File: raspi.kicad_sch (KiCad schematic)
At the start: 0 parts

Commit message: Updated schematics
Added the input current sense, expansion header and various test points.
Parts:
- added J8: Conn_01x03, symbol Connector_Generic:Conn_01x03
- added R24, R25, R26, R27: 0, symbol Device:R_Small_US
- added U6: RP2350B-QFN80, symbol rp2350b-qfn80:RP2350B-QFN80
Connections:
- new net Debug_RX: J8.1 (Pin_1), R24.2
- new net Debug_TX: J8.2 (Pin_2), R25.1
- new net Expansion_RX: R26.1
- new net Expansion_TX: R27.2
- new net GND: J8.3 (Pin_3)
- new net Raspi_RX: R24.1, R27.1
- new net Raspi_TX: R25.2, R26.2

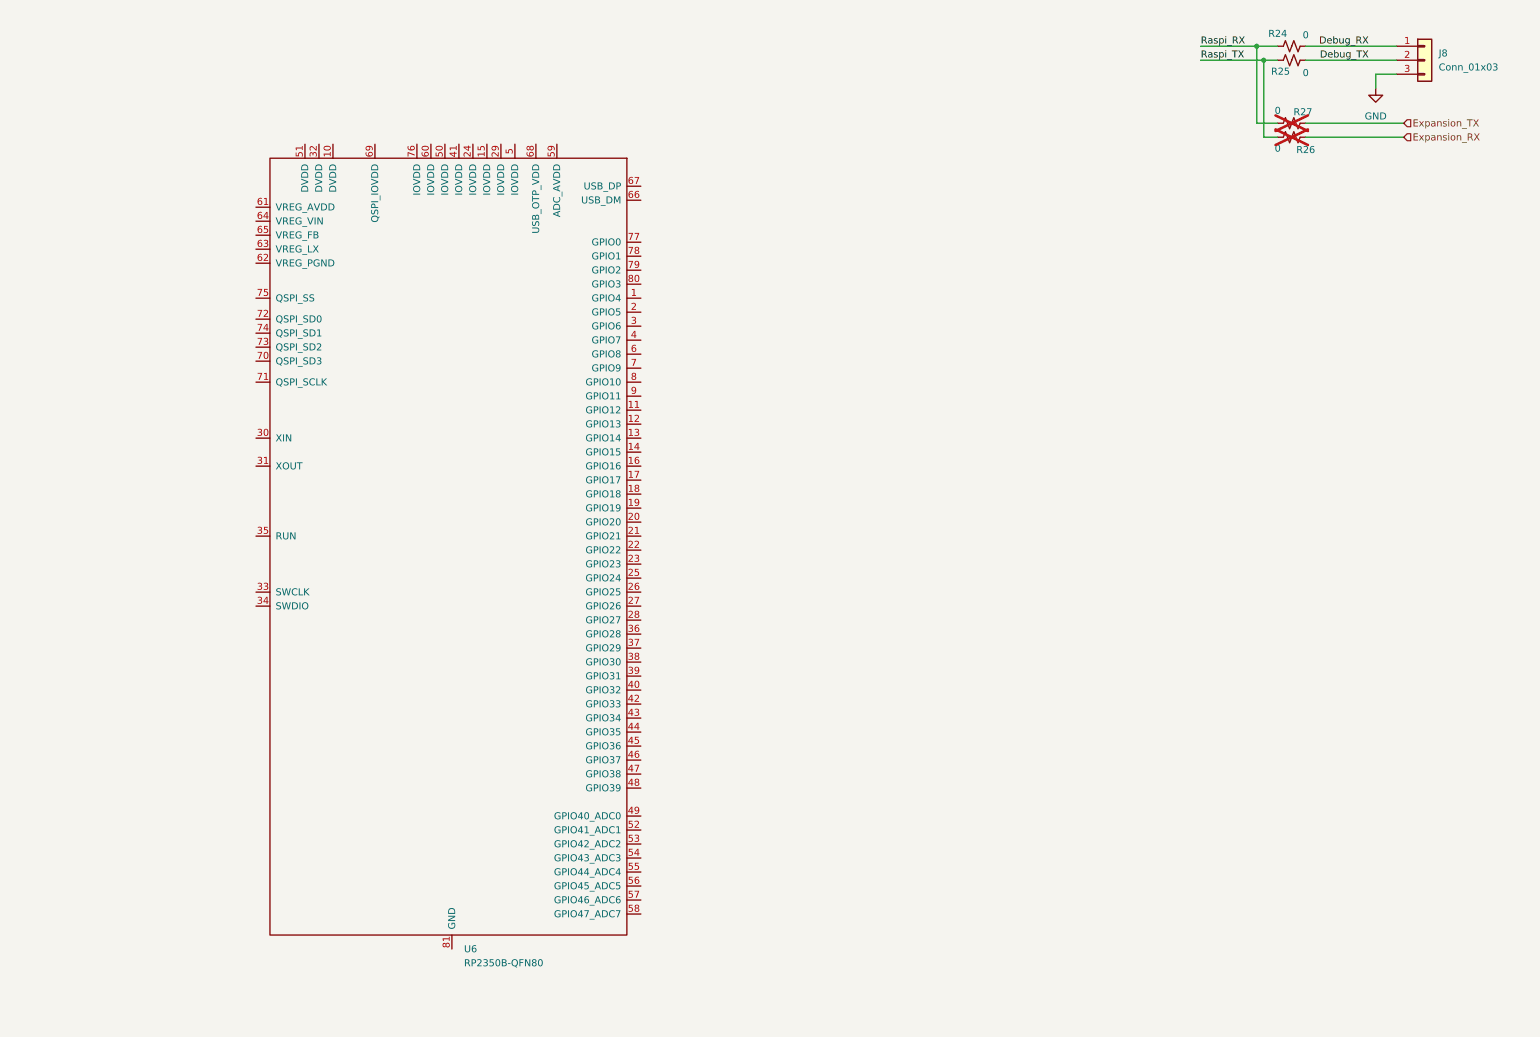
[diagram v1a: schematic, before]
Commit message: Added RPI stuff
Added power passives and usb passives
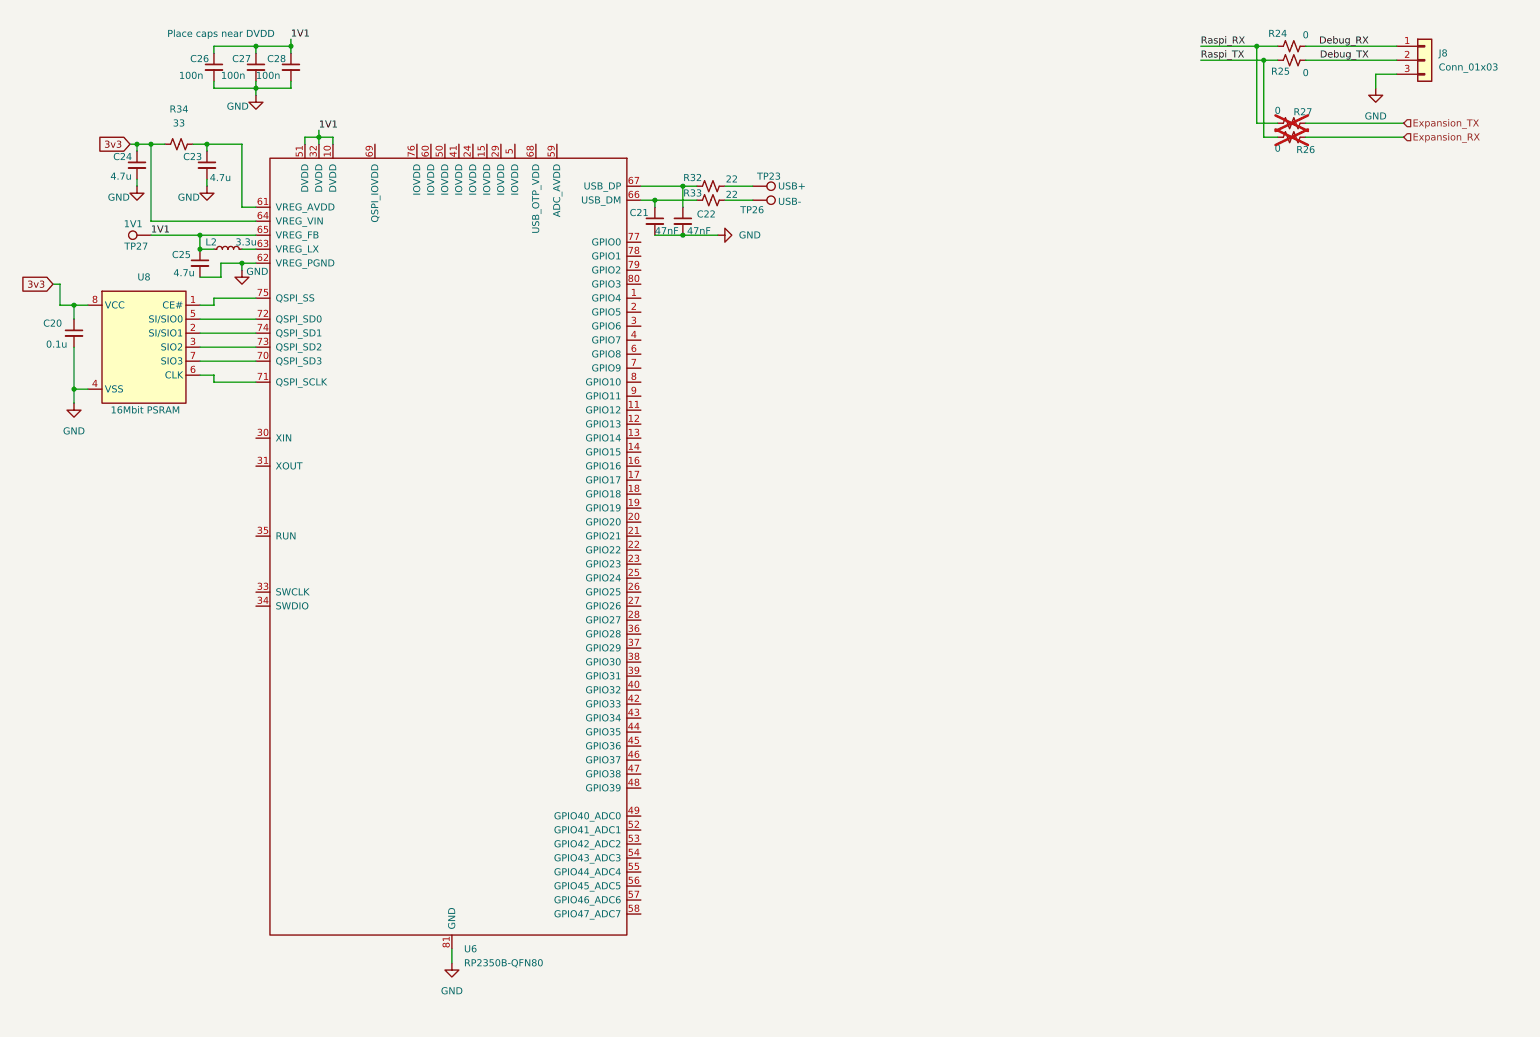
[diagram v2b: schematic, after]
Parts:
- added C20: 0.1u, symbol Device:C_Small
- added C21, C22: 47nF, symbol Device:C_Small
- added C23, C24, C25: 4.7u, symbol Device:C_Small
- added C26, C27, C28: 100n, symbol Device:C_Small
- added L2: 3.3u, symbol Device:L_Small
- added R32, R33: 22, symbol Device:R_Small_US
- added R34: 33, symbol Device:R_Small_US
- added TP23: USB+, symbol Connector:TestPoint
- added TP26: USB-, symbol Connector:TestPoint
- added TP27: 1V1, symbol Connector:TestPoint
- added U8: 16Mbit PSRAM, symbol IS6xWVS2M8xLL:IS6xWVS2M8xLL
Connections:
- net GND: now also U6.62 (VREG_PGND), U6.81 (GND), C20.2, C21.2, C22.2, C23.2, C24.2, C25.2, C26.2, C27.2, C28.2, U8.4 (VSS)
- net 1V1: now reaches U6.10 (DVDD)
- net 1V1: now also U6.32 (DVDD), U6.51 (DVDD), U6.65 (VREG_FB), C25.1, C26.1, C27.1, C28.1, L2.1, TP27.1
- net at U6.61 (VREG_AVDD): now also C23.1, R34.2
- net at U6.63 (VREG_LX): now also L2.2
- net 3v3: now reaches U6.64 (VREG_VIN)
- net 3v3: now also C20.1, C24.1, R34.1, U8.8 (VCC)
- net at U6.66 (USB_DM): now also C21.1, R33.1
- net at U6.67 (USB_DP): now also C22.1, R32.1
- net at U6.70 (QSPI_SD3): now also U8.7 (SIO3)
- net at U6.71 (QSPI_SCLK): now also U8.6 (CLK)
- net at U6.72 (QSPI_SD0): now also U8.5 (SI/SIO0)
- net at U6.73 (QSPI_SD2): now also U8.3 (SIO2)
- net at U6.74 (QSPI_SD1): now also U8.2 (SI/SIO1)
- net at U6.75 (QSPI_SS): now also U8.1 (CE#)
- new net: R32.2, TP23.1
- new net: R33.2, TP26.1
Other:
- note added: "Place caps near DVDD"

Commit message: Setup top sheet
Added TVS diodes, updated top sheet, misc label fixes
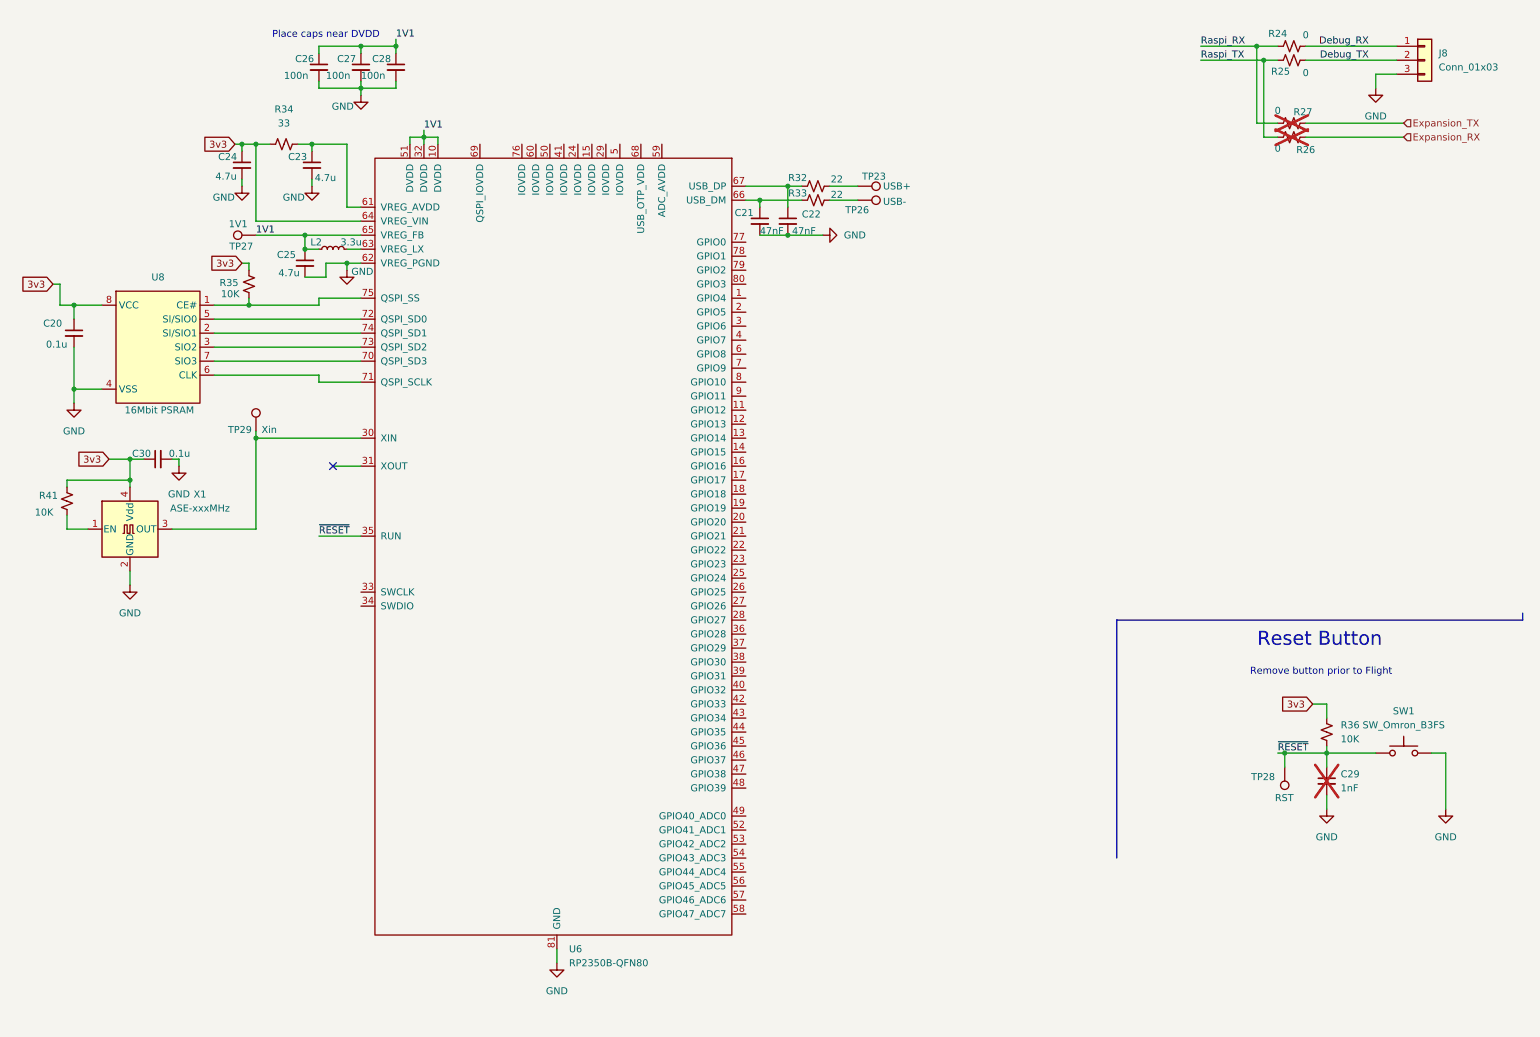
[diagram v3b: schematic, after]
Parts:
- added C29: 1nF, symbol Device:C_Small
- added C30: 0.1u, symbol Device:C_Small
- added R35, R36, R41: 10K, symbol Device:R_Small_US
- added SW1: SW_Omron_B3FS, symbol Switch:SW_Omron_B3FS
- added TP28: RST, symbol Connector:TestPoint
- added TP29: Xin, symbol Connector:TestPoint
- added X1: ASE-xxxMHz, Oscillator:Oscillator_SMD_Abracon_ASE-4Pin_3.2x2.5mm, symbol Oscillator:ASE-xxxMHz
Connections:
- net 3v3: now also C30.1, R35.1, R36.1, R41.1, X1.4 (Vdd)
- net GND: now also C29.2, C30.2, SW1.2, X1.2 (GND)
- net at U6.30 (XIN): now also TP29.1, X1.3 (OUT)
- net ~{RESET}: now reaches U6.35 (RUN)
- net ~{RESET}: now also C29.1, R36.2, SW1.1, TP28.1
- net at U6.75 (QSPI_SS), U8.1 (CE#): now also R35.2
- new net: R41.2, X1.1 (EN)
- no-connect marks 0 -> 1
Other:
- note added: "Remove button prior to Flight"
- note added: "Reset Button"
- moved on the sheet: C21, C22, C23, C24, C25, C26, C27, C28, L2, R32, R33, R34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

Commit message: Updated Raspi Sheet
Added hierarchical labels and misc additions.
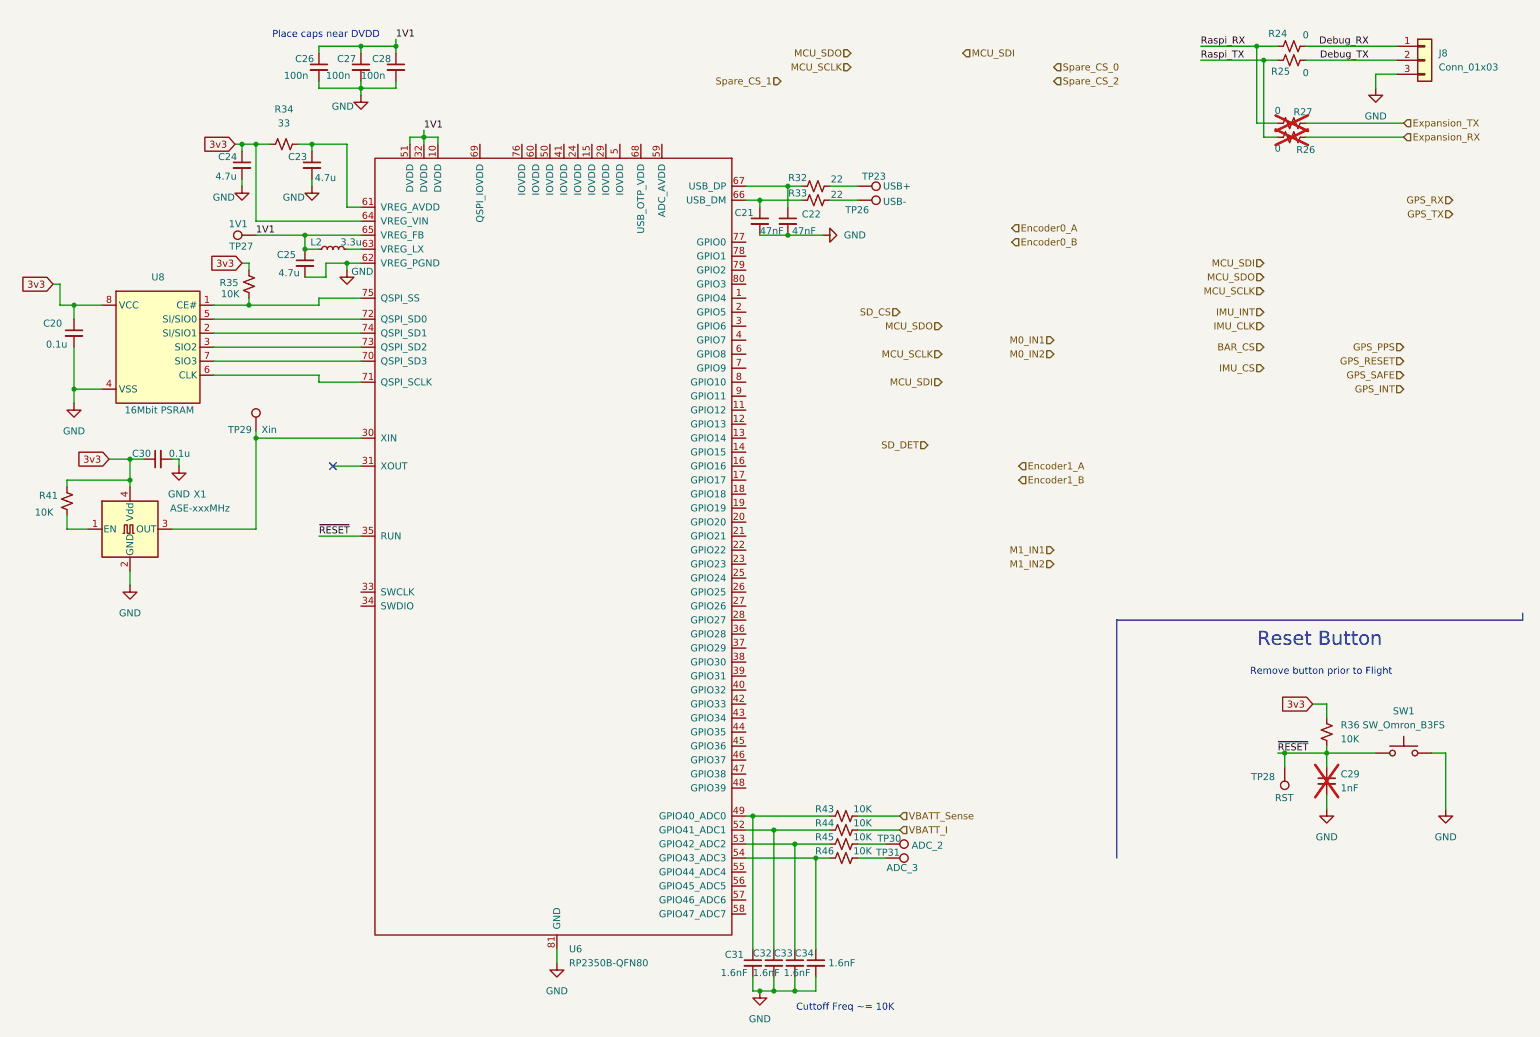
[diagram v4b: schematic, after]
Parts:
- added C31, C32, C33, C34: 1.6nF, symbol Device:C_Small
- added R43, R44, R45, R46: 10K, symbol Device:R_Small_US
- added TP30: ADC_2, symbol Connector:TestPoint
- added TP31: ADC_3, symbol Connector:TestPoint
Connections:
- net GND: now also C31.2, C32.2, C33.2, C34.2
- net at U6.49 (GPIO40_ADC0): now also C31.1, R43.1
- net at U6.52 (GPIO41_ADC1): now also C32.1, R44.1
- net at U6.53 (GPIO42_ADC2): now also C33.1, R45.1
- net at U6.54 (GPIO43_ADC3): now also C34.1, R46.1
- new net: R45.2, TP30.1
- new net: R46.2, TP31.1
- new net VBATT_I: R44.2
- new net VBATT_Sense: R43.2
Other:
- note added: "Cuttoff Freq ~= 10K"

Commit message: Updated MCU pinout
Added bypass caps and started assigning pinouts.
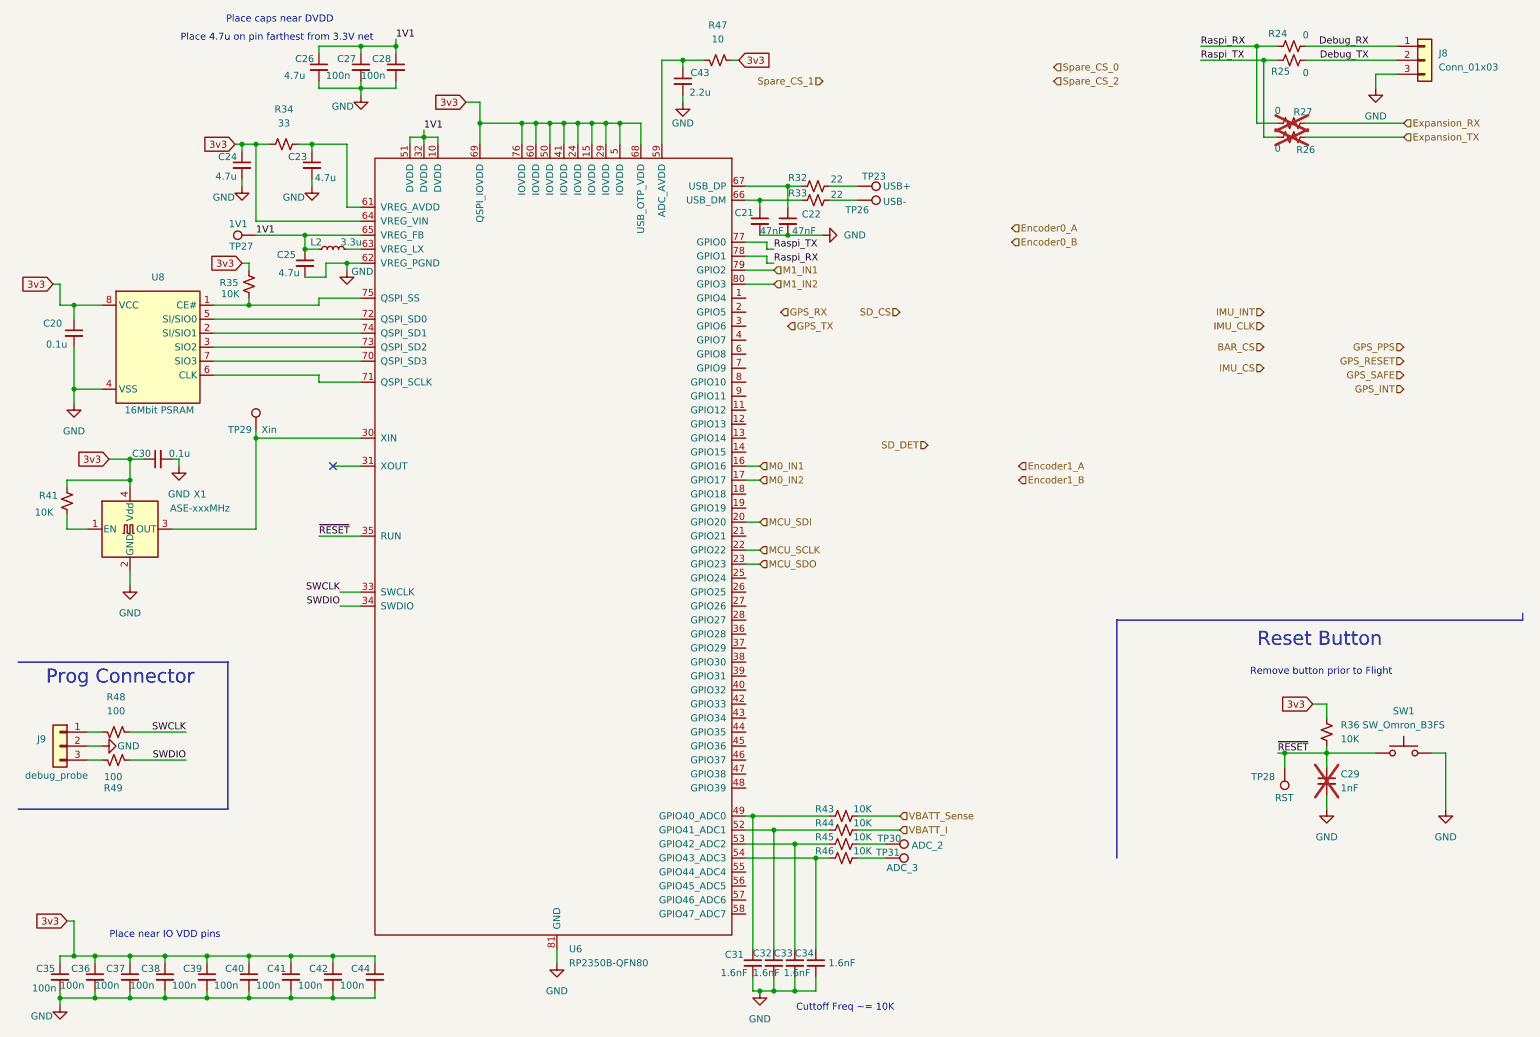
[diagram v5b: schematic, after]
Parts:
- added C35, C36, C37, C38, C39, C40, C41, C42, C44: 100n, symbol Device:C_Small
- added C43: 2.2u, symbol Device:C_Small
- added J9: debug_probe, symbol Connector_Generic:Conn_01x03
- added R47: 10, symbol Device:R_Small_US
- added R48, R49: 100, symbol Device:R_Small_US
- C26: value 100n -> 4.7u
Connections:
- net 3v3: now also U6.15 (IOVDD), U6.24 (IOVDD), U6.29 (IOVDD), U6.41 (IOVDD), U6.5 (IOVDD), U6.50 (IOVDD), U6.60 (IOVDD), U6.68 (USB_OTP_VDD), U6.69 (QSPI_IOVDD), U6.76 (IOVDD), C35.1, C36.1, C37.1, C38.1, C39.1, C40.1, C41.1, C42.1, C44.1, R47.1
- net Expansion_RX: now also R27.2; no longer R26.1
- net Expansion_TX: now also R26.1; no longer R27.2
- net GND: now also C35.2, C36.2, C37.2, C38.2, C39.2, C40.2, C41.2, C42.2, C43.2, C44.2, J9.2 (Pin_2)
- net M0_IN1: now also U6.16 (GPIO16)
- net M0_IN2: now also U6.17 (GPIO17)
- net M1_IN1: now also U6.79 (GPIO2)
- net M1_IN2: now also U6.80 (GPIO3)
- net MCU_SCLK: now also U6.22 (GPIO22)
- net MCU_SDI: now also U6.20 (GPIO20)
- net MCU_SDO: now also U6.23 (GPIO23)
- net Raspi_RX: now also U6.78 (GPIO1)
- net Raspi_TX: now also U6.77 (GPIO0)
- net SWCLK: now reaches U6.33 (SWCLK)
- net SWCLK: now also R48.1
- net SWDIO: now reaches U6.34 (SWDIO)
- net SWDIO: now also R49.1
- net at U6.59 (ADC_AVDD): now also C43.1, R47.2
- new net: J9.3 (Pin_3), R49.2
- new net: J9.1 (Pin_1), R48.2
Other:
- note added: "Place 4.7u on pin farthest from 3.3V net"
- note added: "Place near IO VDD pins"
- note added: "Prog Connector"
